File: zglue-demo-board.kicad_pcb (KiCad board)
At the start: 6 copper layers, 56 x 66 mm, 102 parts, among them J10 0473460001, J2 DF13A-2P-1.25H, J3 20021121-00010C4LF, J4 2x20_Header_Female, J5 0473460001, J6 556500488, J7 556500488, J8 WE_686115148922, J9 WE_686115148922_FLIPPED, U1 MCP1700T-3302E_TT, U2 NTB0104BQ, U3 NTB0104BQ, U4 NTB0104BQ, U5 93LC56CT-IMC, U6 FT4232HQ, Y1 ASFLMB-12.000MHZ-LC-T

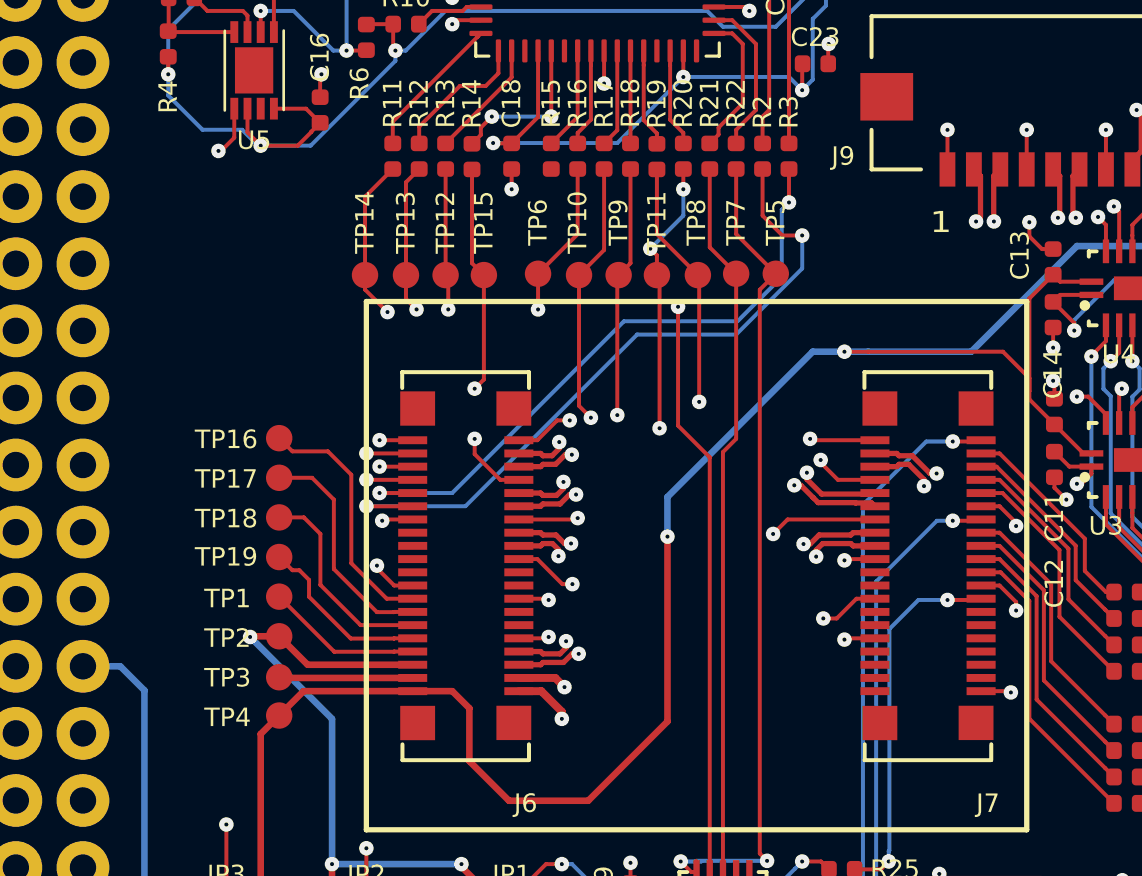
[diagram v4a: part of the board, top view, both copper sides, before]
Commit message: added programming header for QSPI flash
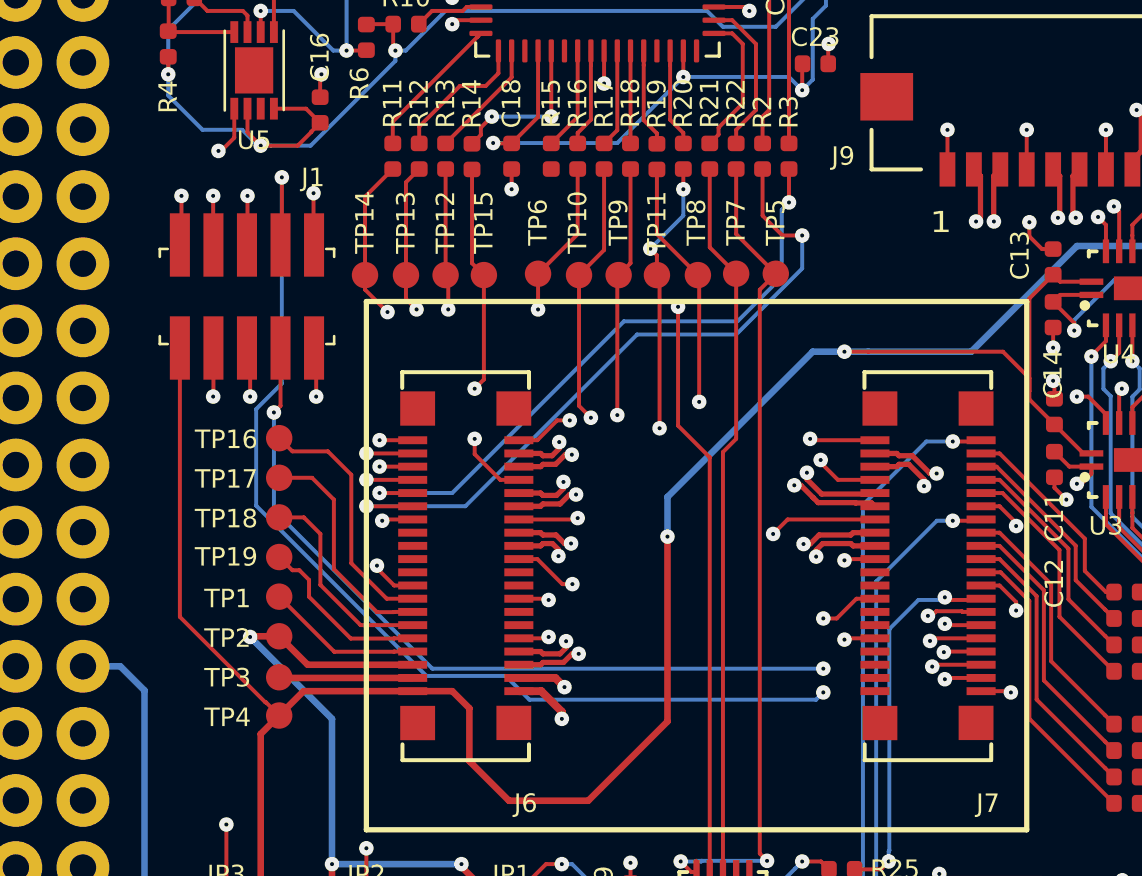
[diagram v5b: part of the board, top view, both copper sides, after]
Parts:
- added J1: 20021121-00010C4LF, antmicro-footprints:PinHeader_2x5_P1.27mm, F.Cu at (11.0, 22.8)
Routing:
- net /FLASH_IO3: track 0.00 -> 46.2 mm, vias 0 -> 3
- net /FLASH_CS: track 0.00 -> 42.9 mm, vias 0 -> 2
- net /FLASH_IO1: track 0.00 -> 42.7 mm, vias 0 -> 2
- net /CTRL_RST_FLASH_SOC_CS: track 20.6 -> 60.9 mm, vias 2 -> 3
- net /FLASH_IO2: track 0.00 -> 35.6 mm, vias 0 -> 3
- net /DONE: track 14.2 -> 49.2 mm, vias 2 -> 3
- net /FLASH_IO0: track 0.00 -> 34.4 mm, vias 0 -> 2
- net /FLASH_CLK: track 0.00 -> 30.8 mm, vias 0 -> 2
- net /3V3_SYS: track 192.0 -> 207.5 mm
- net GND: track 135.8 -> 137.6 mm, vias 77 -> 78

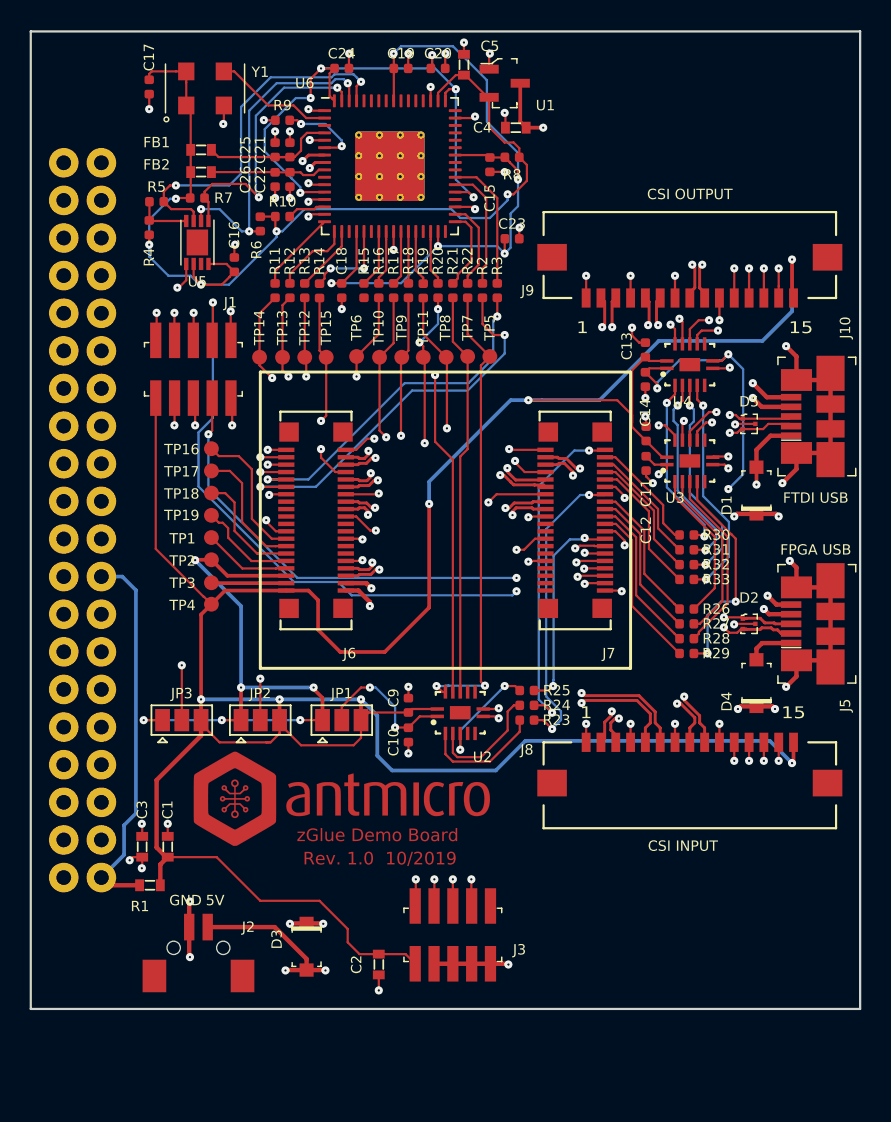
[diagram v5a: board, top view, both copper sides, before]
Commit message: added LEDs and power button
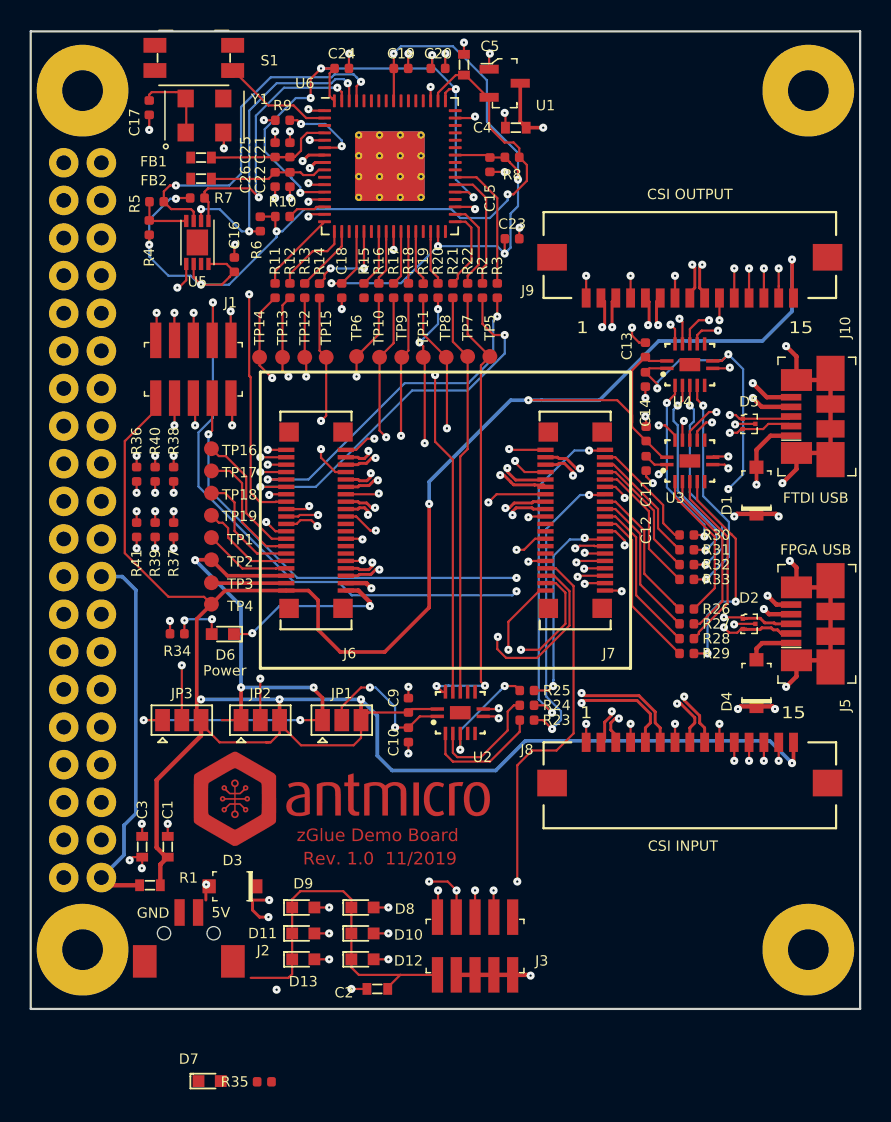
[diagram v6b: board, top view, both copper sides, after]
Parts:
- added D10: LG_L29K-G2J1-24-Z, antmicro-footprints:LED_0603, F.Cu at (22.4, 59.1)
- added D11: LG_L29K-G2J1-24-Z, antmicro-footprints:LED_0603, F.Cu at (18.4, 60.9)
- added D12: LG_L29K-G2J1-24-Z, antmicro-footprints:LED_0603, F.Cu at (22.4, 62.6)
- added D13: LG_L29K-G2J1-24-Z, antmicro-footprints:LED_0603, F.Cu at (18.4, 62.6)
- added D6: LG_L29K-G2J1-24-Z, antmicro-footprints:LED_0603, F.Cu at (13.0, 40.7)
- added D7: LG_L29K-G2J1-24-Z, antmicro-footprints:LED_0603, F.Cu at (12.1, 70.9)
- added D8: LG_L29K-G2J1-24-Z, antmicro-footprints:LED_0603, F.Cu at (22.4, 60.9)
- added D9: LG_L29K-G2J1-24-Z, antmicro-footprints:LED_0603, F.Cu at (18.4, 59.1)
- added R34: R_470R_0402, antmicro-footprints:0402-res, F.Cu at (9.89, 40.7)
- added R35: R_330R_0402, antmicro-footprints:0402-res, F.Cu at (15.8, 70.9)
- added R36: R_330R_0402, antmicro-footprints:0402-res, F.Cu at (7.15, 29.9)
- added R37: R_330R_0402, antmicro-footprints:0402-res, F.Cu at (9.65, 33.6)
- added R38: R_330R_0402, antmicro-footprints:0402-res, F.Cu at (9.65, 29.9)
- added R39: R_330R_0402, antmicro-footprints:0402-res, F.Cu at (8.40, 33.6)
- added R40: R_330R_0402, antmicro-footprints:0402-res, F.Cu at (8.40, 29.9)
- added R41: R_330R_0402, antmicro-footprints:0402-res, F.Cu at (7.15, 33.6)
- added REF**: Mount-hole-M2.5, antmicro-footprints:Mount-hole-M2.5, F.Cu at (-13.3, 2.80)
- added REF**: Mount-hole-M2.5, antmicro-footprints:Mount-hole-M2.5, F.Cu at (-9.40, 62.7)
- added REF**: Mount-hole-M2.5, antmicro-footprints:Mount-hole-M2.5, F.Cu at (51.8, 62.1)
- added REF**: Mount-hole-M2.5, antmicro-footprints:Mount-hole-M2.5, F.Cu at (51.9, 3.92)
- added S1: EVQPUA02K, antmicro-footprints:Panasonic_EVQPUJ_EVQPUA, F.Cu at (11.0, 1.79)
- moved D3 6.46 mm to (13.6, 57.7), turned to 180 degrees
- moved Y1 1.83 mm to (10.5, 6.83)
- moved J3 1.68 mm to (30.0, 61.8)
- moved C2 1.65 mm to (23.4, 64.7), turned to 180 degrees
- moved C17 1.40 mm to (8.00, 5.15)
- moved J2 1.18 mm to (10.1, 59.5)
- moved FB1 0.52 mm to (11.5, 8.52)
- moved FB2 0.44 mm to (11.5, 9.94)
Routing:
- net /CTRL_OUT: track 0.00 -> 45.3 mm, vias 0 -> 2
- net Net-(D8-Pad2): track 0.00 -> 41.5 mm, vias 0 -> 2
- net Net-(D12-Pad2): track 0.00 -> 40.5 mm, vias 0 -> 2
- net /PROC_OUT_0: track 0.00 -> 37.6 mm, vias 0 -> 2
- net Net-(D10-Pad2): track 0.00 -> 37.3 mm, vias 0 -> 2
- net /PROC_OUT_1: track 0.00 -> 37.1 mm, vias 0 -> 2
- net /PROC_OUT_2: track 0.00 -> 35.8 mm, vias 0 -> 2
- net Net-(D13-Pad2): track 0.00 -> 34.9 mm, vias 0 -> 2
- net Net-(D11-Pad2): track 0.00 -> 32.7 mm, vias 0 -> 2
- net Net-(D9-Pad2): track 0.00 -> 31.8 mm, vias 0 -> 2
- net /LED1_ISINK: track 0.00 -> 16.7 mm, vias 0 -> 2
- net /LED3_ISINK: track 0.00 -> 16.3 mm, vias 0 -> 2
- net /PWR_BTN: track 0.00 -> 16.1 mm, vias 0 -> 1
- net /LED2_ISINK: track 0.00 -> 14.6 mm, vias 0 -> 2
- net /VUSB: track 12.2 -> 22.9 mm, vias 8 -> 9
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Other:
- board text added: "Power"
- board text added: "Rev. 1.0 11/2019"
- board text removed: "Rev. 1.0 10/2019"

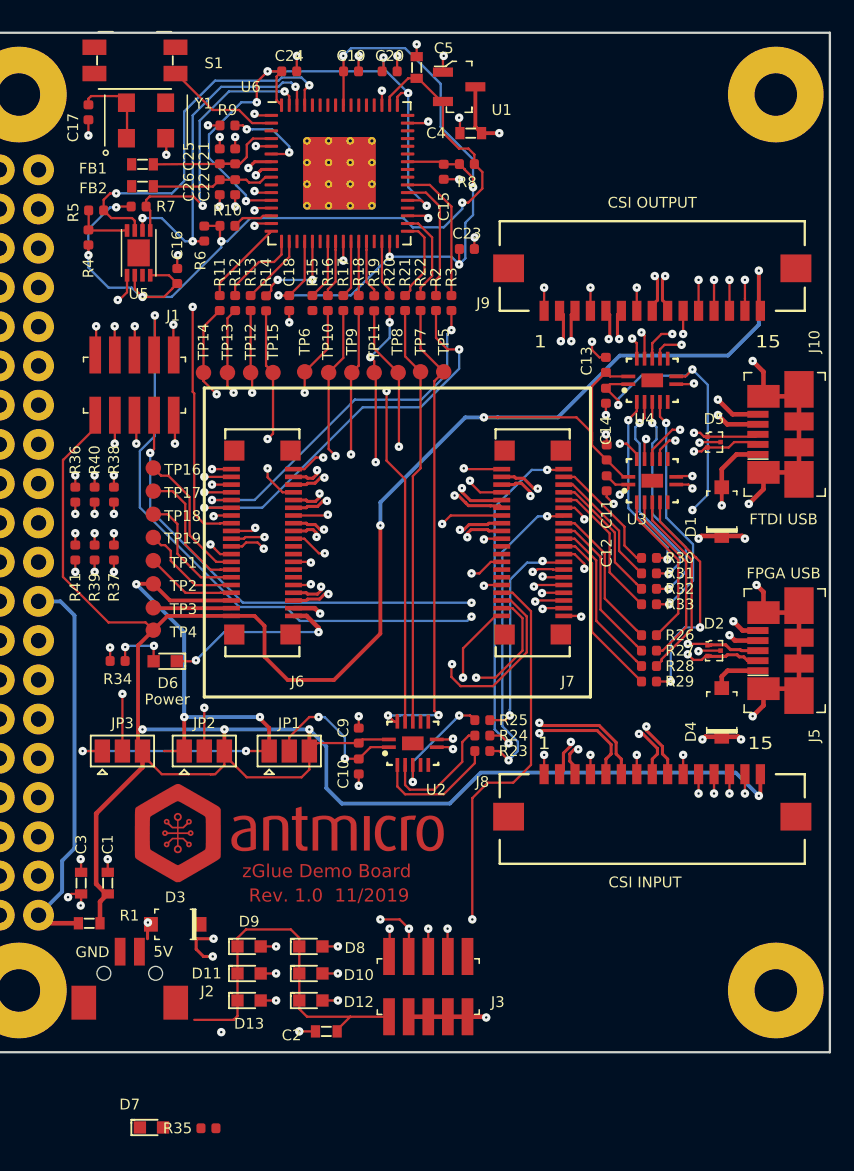
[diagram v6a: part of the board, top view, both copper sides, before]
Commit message: Added mounting holes
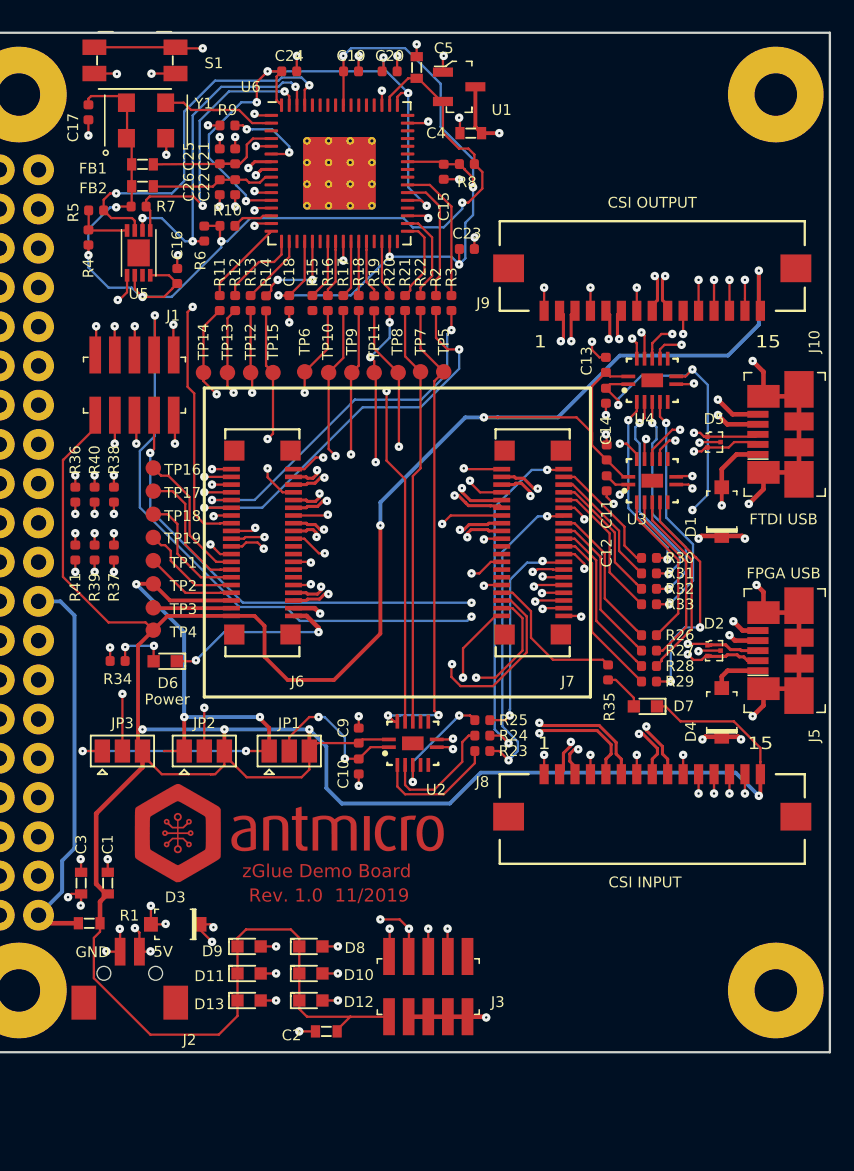
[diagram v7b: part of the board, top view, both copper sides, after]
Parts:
- removed the REF** at (-13.3, 2.80)
- removed the REF** at (-9.40, 62.7)
- removed the REF** at (51.8, 62.1)
- removed the REF** at (51.9, 3.92)
- added REF**: Mount-hole-M2.5, antmicro-footprints:Mount-hole-M2.5, F.Cu at (3.50, 4.00)
- added REF**: Mount-hole-M2.5, antmicro-footprints:Mount-hole-M2.5, F.Cu at (3.50, 62.0)
- added REF**: Mount-hole-M2.5, antmicro-footprints:Mount-hole-M2.5, F.Cu at (52.5, 62.0)
- added REF**: Mount-hole-M2.5, antmicro-footprints:Mount-hole-M2.5, F.Cu at (52.5, 4.00)
- moved D7 42.0 mm to (44.1, 43.6), turned to 180 degrees
- moved R35 39.2 mm to (41.6, 41.4), turned to 90 degrees
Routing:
- net /CTRL_OUT: track 45.3 -> 9.83 mm, vias 2 -> 0
- net /PWR_BTN: track 16.1 -> 41.5 mm, vias 1 -> 2
- net /3V3_SYS: track 215.0 -> 236.6 mm
- net GND: track 134.6 -> 140.7 mm, vias 77 -> 81
- net /3V3_FTDI: track 63.4 -> 67.9 mm
- net /5V0_IN: track 2.75 -> 6.28 mm, vias 3 -> 6
- net Net-(D7-Pad2): track 0.00 -> 2.70 mm
- net /VUSB: track 22.9 -> 22.3 mm
- net (no net): track 0.55 -> 0.00 mm
